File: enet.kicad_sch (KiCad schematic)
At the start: 32 parts

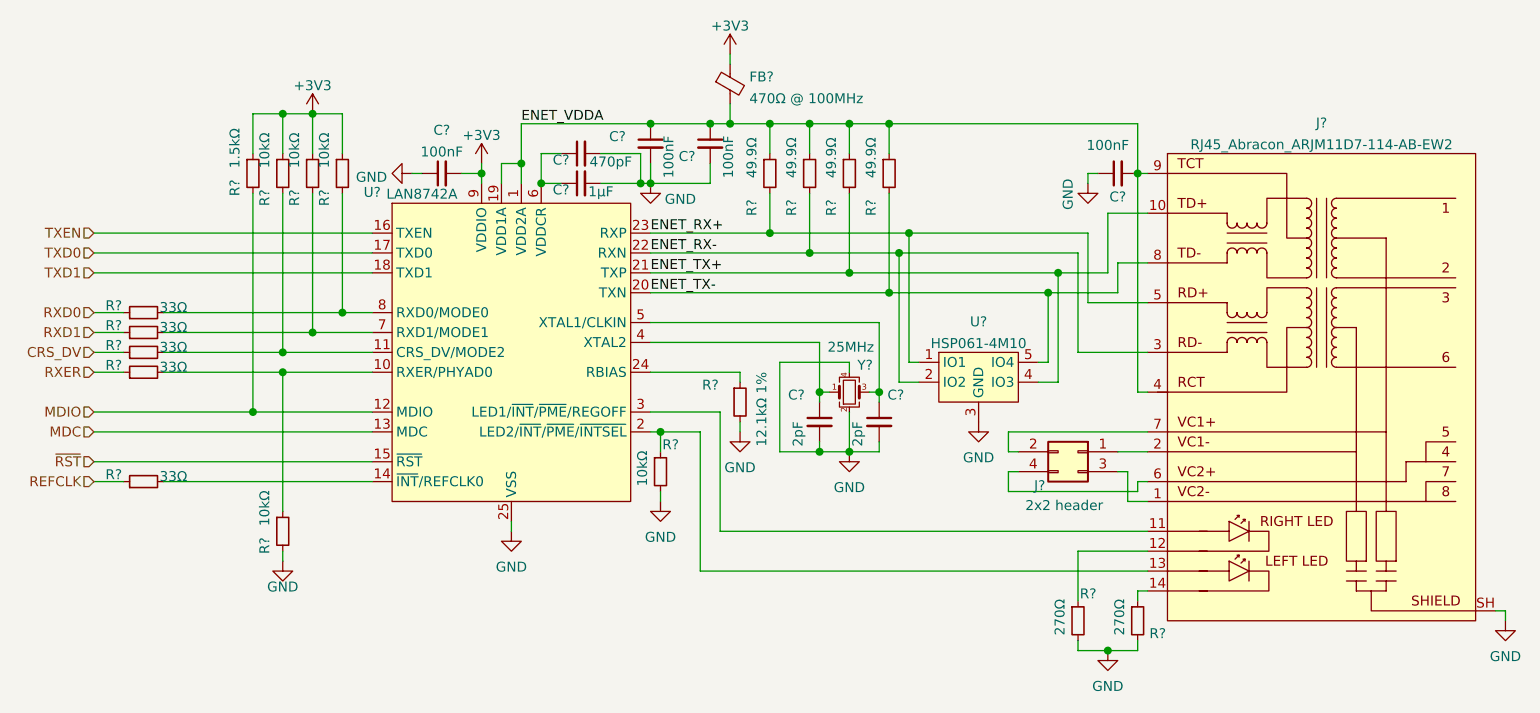
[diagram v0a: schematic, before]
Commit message: Some PSU changes, add new solder jumper symbol
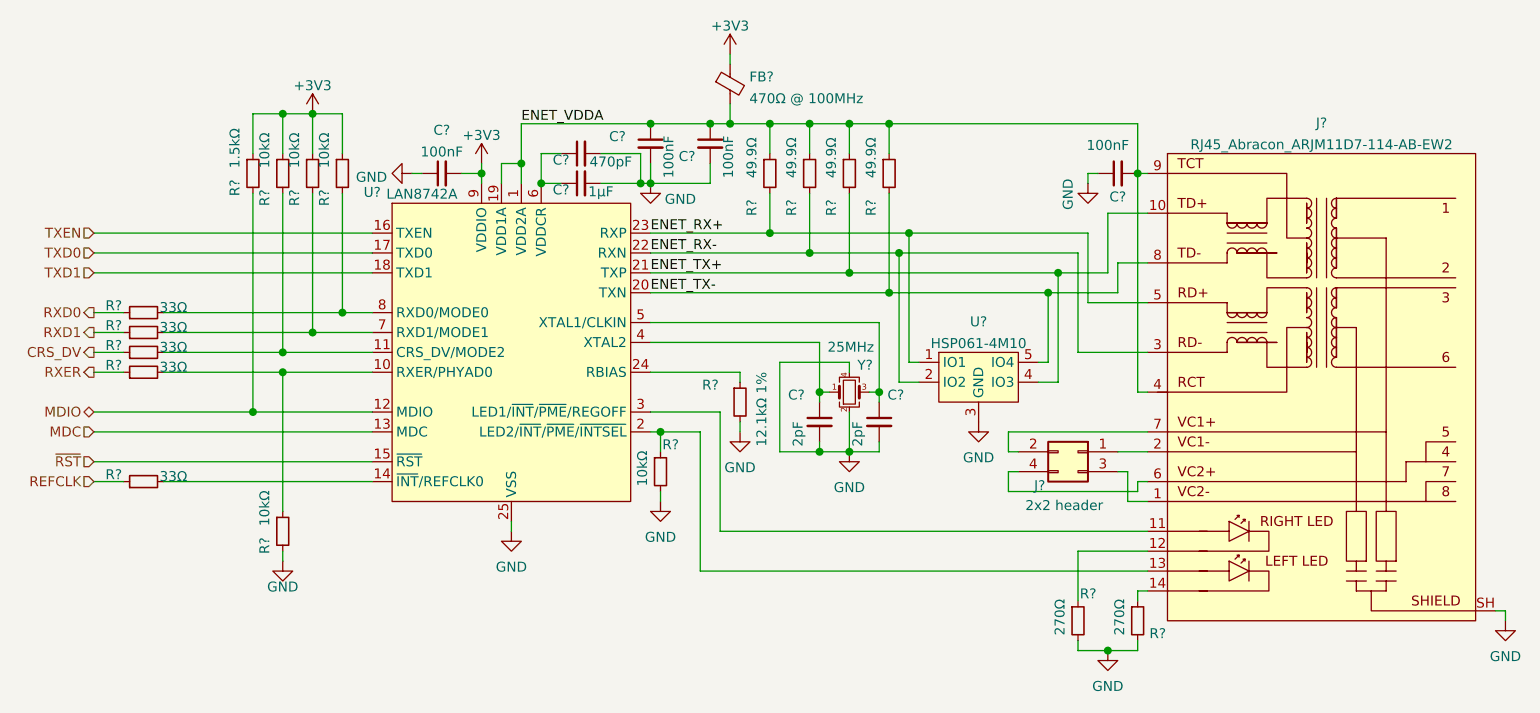
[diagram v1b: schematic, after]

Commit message: Add microSD card and annotate mostly complete schematic
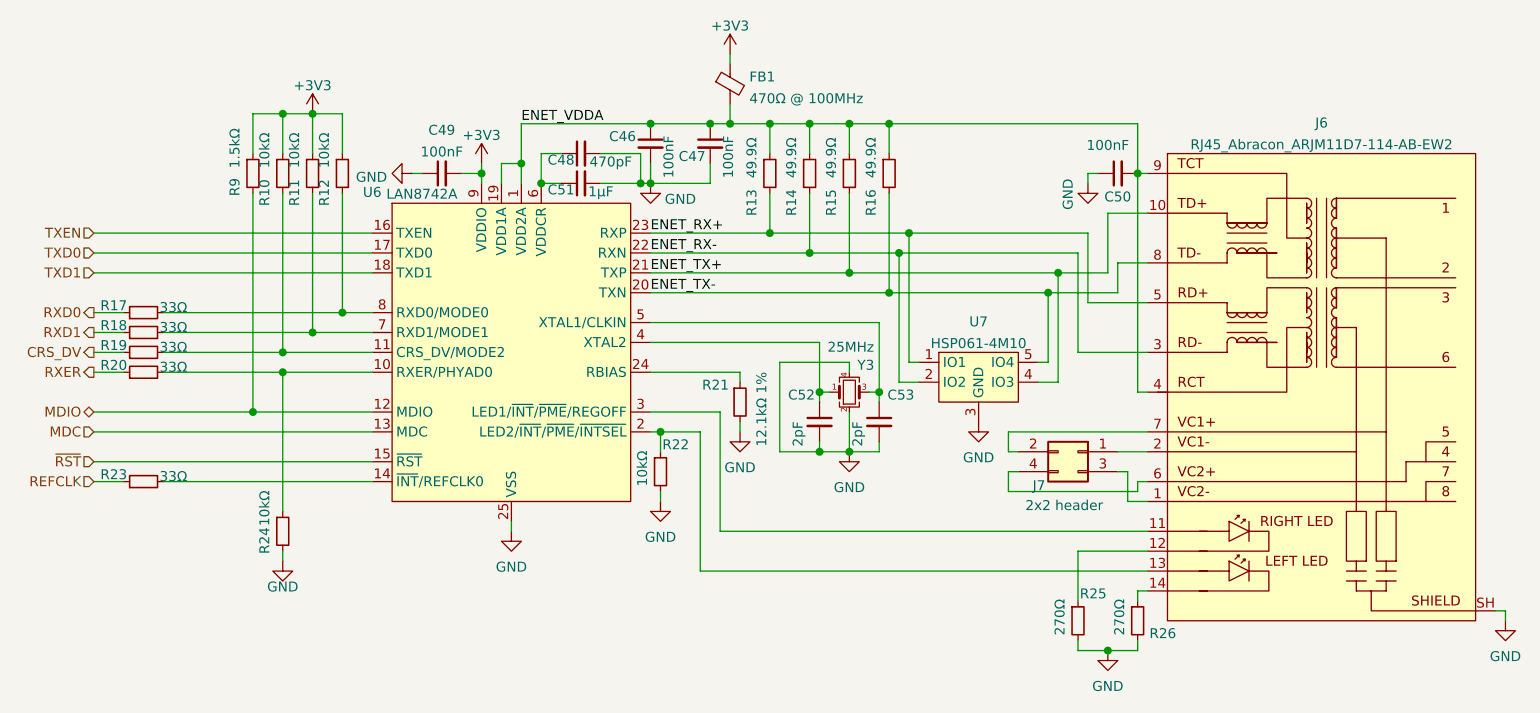
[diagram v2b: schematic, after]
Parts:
- C46, C47, C48, C49, C51, C52, C53: renamed from C?; footprint (none) -> Capacitor_SMD:C_0402_1005Metric
- FB1: renamed from FB?; footprint (none) -> Inductor_SMD:L_0603_1608Metric
- R10, R11, R12, R13, R14, R15, R16, R17, R18, R19, R20, R21, R22, R23, R24, R25, R26, R9: renamed from R?; footprint (none) -> Resistor_SMD:R_0402_1005Metric
- gave numbers to parts that had none: 6

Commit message: YOU CAN'T CUT BACK ON DECOUPLING CAPACITORS! YOU WILL REGRET THIS!
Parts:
- C50: footprint Capacitor_SMD:C_0603_1608Metric -> Capacitor_SMD:C_0402_1005Metric
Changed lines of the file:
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@@
     (company "Design by Artemis Tosini <me@artem.ist>")
   )
+  (junction (at 152.4 78.74) (diameter 1.016) (color 0 0 0 0))
   (junction (at 147.32 62.23) (diameter 1.016) (color 0 0 0 0))
+  (junction (at 157.48 104.14) (diameter 1.016) (color 0 0 0 0))
+  (junction (at 142.24 62.23) (diameter 1.016) (color 0 0 0 0))
+  (junction (at 163.83 78.74) (diameter 1.016) (color 0 0 0 0))
+  (junction (at 92.71 86.36) (diameter 1.016) (color 0 0 0 0))
+  (junction (at 130.81 69.85) (diameter 1.016) (color 0 0 0 0))
+  (junction (at 157.48 81.28) (diameter 1.016) (color 0 0 0 0))
+  (junction (at 133.35 101.6) (diameter 1.016) (color 0 0 0 0))
+  (junction (at 81.28 99.06) (diameter 1.016) (color 0 0 0 0))
+  (junction (at 162.56 62.23) (diameter 1.016) (color 0 0 0 0))
+  (junction (at 165.1 76.2) (diameter 1.016) (color 0 0 0 0))
+  (junction (at 157.48 62.23) (diameter 1.016) (color 0 0 0 0))
+  (junction (at 132.08 69.85) (diameter 1.016) (color 0 0 0 0))
+  (junction (at 118.11 69.85) (diameter 1.016) (color 0 0 0 0))
+  (junction (at 190.5 129.54) (diameter 1.016) (color 0 0 0 0))
+  (junction (at 85.09 93.98) (diameter 1.016) (color 0 0 0 0))
+  (junction (at 162.56 83.82) (diameter 1.016) (color 0 0 0 0))
+  (junction (at 110.49 68.58) (diameter 1.016) (color 0 0 0 0))
+  (junction (at 147.32 76.2) (diameter 1.016) (color 0 0 0 0))
+  (junction (at 161.29 96.52) (diameter 1.016) (color 0 0 0 0))
+  (junction (at 139.7 62.23) (diameter 1.016) (color 0 0 0 0))
+  (junction (at 132.08 62.23) (diameter 1.016) (color 0 0 0 0))
+  (junction (at 152.4 62.23) (diameter 1.016) (color 0 0 0 0))
+  (junction (at 88.9 60.96) (diameter 1.016) (color 0 0 0 0))
+  (junction (at 153.67 104.14) (diameter 1.016) (color 0 0 0 0))
+  (junction (at 182.88 83.82) (diameter 1.016) (color 0 0 0 0))
+  (junction (at 88.9 88.9) (diameter 1.016) (color 0 0 0 0))
+  (junction (at 85.09 91.44) (diameter 1.016) (color 0 0 0 0))
+  (junction (at 85.09 60.96) (diameter 1.016) (color 0 0 0 0))
+  (junction (at 153.67 96.52) (diameter 1.016) (color 0 0 0 0))
   (junction (at 115.57 67.31) (diameter 1.016) (color 0 0 0 0))
-  (junction (at 163.83 78.74) (diameter 1.016) (color 0 0 0 0))
+  (junction (at 184.15 81.28) (diameter 1.016) (color 0 0 0 0))
   (junction (at 194.31 68.58) (diameter 1.016) (color 0 0 0 0))
-  (junction (at 132.08 69.85) (diameter 1.016) (color 0 0 0 0))
-  (junction (at 182.88 83.82) (diameter 1.016) (color 0 0 0 0))
-  (junction (at 118.11 69.85) (diameter 1.016) (color 0 0 0 0))
-  (junction (at 81.28 99.06) (diameter 1.016) (color 0 0 0 0))
-  (junction (at 153.67 96.52) (diameter 1.016) (color 0 0 0 0))
-  (junction (at 92.71 86.36) (diameter 1.016) (color 0 0 0 0))
-  (junction (at 184.15 81.28) (diameter 1.016) (color 0 0 0 0))
-  (junction (at 139.7 62.23) (diameter 1.016) (color 0 0 0 0))
-  (junction (at 88.9 88.9) (diameter 1.016) (color 0 0 0 0))
-  (junction (at 157.48 104.14) (diameter 1.016) (color 0 0 0 0))
-  (junction (at 85.09 60.96) (diameter 1.016) (color 0 0 0 0))
-  (junction (at 190.5 129.54) (diameter 1.016) (color 0 0 0 0))
-  (junction (at 165.1 76.2) (diameter 1.016) (color 0 0 0 0))
-  (junction (at 110.49 68.58) (diameter 1.016) (color 0 0 0 0))
-  (junction (at 152.4 62.23) (diameter 1.016) (color 0 0 0 0))
-  (junction (at 161.29 96.52) (diameter 1.016) (color 0 0 0 0))
-  (junction (at 130.81 69.85) (diameter 1.016) (color 0 0 0 0))
-  (junction (at 85.09 93.98) (diameter 1.016) (color 0 0 0 0))
-  (junction (at 162.56 62.23) (diameter 1.016) (color 0 0 0 0))
-  (junction (at 142.24 62.23) (diameter 1.016) (color 0 0 0 0))
-  (junction (at 153.67 104.14) (diameter 1.016) (color 0 0 0 0))
-  (junction (at 133.35 101.6) (diameter 1.016) (color 0 0 0 0))
-  (junction (at 147.32 76.2) (diameter 1.016) (color 0 0 0 0))
-  (junction (at 88.9 60.96) (diameter 1.016) (color 0 0 0 0))
-  (junction (at 162.56 83.82) (diameter 1.016) (color 0 0 0 0))
-  (junction (at 152.4 78.74) (diameter 1.016) (color 0 0 0 0))
-  (junction (at 85.09 91.44) (diameter 1.016) (color 0 0 0 0))
-  (junction (at 157.48 81.28) (diameter 1.016) (color 0 0 0 0))
-  (junction (at 132.08 62.23) (diameter 1.016) (color 0 0 0 0))
-  (junction (at 157.48 62.23) (diameter 1.016) (color 0 0 0 0))
   (wire (pts (xy 140.97 99.06) (xy 140.97 114.3))
     (stroke (width 0) (type solid) (color 0 0 0 0))
@@
     (property "Reference" "C50" (id 0) (at 191.77 71.5687 90))
     (property "Value" "100nF" (id 1) (at 190.5 64.9836 90))
-    (property "Footprint" "Capacitor_SMD:C_0603_1608Metric" (id 2) (at 191.77 68.58 0)
-      (effects (font (size 1.27 1.27)) hide)
-    )
+    (property "Footprint" "Capacitor_SMD:C_0402_1005Metric" (id 2) (at 191.77 68.58 0)
+      (effects (font (size 1.27 1.27)) hide)
+    )

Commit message: Start PCB
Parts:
- renumbered C46 to C37, C47 to C38, C48 to C39, C49 to C40, C50 to C41, C51 to C42, C52 to C43, C53 to C44
